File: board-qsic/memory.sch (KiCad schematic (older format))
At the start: 9 parts, among them U401 XC7A75T-CSG324, U501 IS43TR16128B

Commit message: Reworked board from template.  Changed schematic to let me use the bus drivers and level converters more efficiently so to get all the signals.
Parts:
- removed U401: XC7A75T-CSG324, myMods.pretty:CSG324, symbol myLib:XC7A75T-CSG324
- added C301, C302, C303: 100nF, Capacitor_SMD:C_0603_1608Metric, symbol Device:C_Small
- added U101: XC7A75T-CSG324, Package_BGA:BGA-324_15.0x15.0mm_Layout18x18_P0.8mm_Ball0.5mm_Pad0.4mm_NSMD, symbol FPGA_Xilinx_Artix7:XC7A75T-CSG324
- C304: renamed from C501; footprint Capacitors_SMD:C_0603 -> Capacitor_SMD:C_0603_1608Metric; symbol qsic-rescue:C_Small-device -> Device:C_Small; manf# (none) -> CL10B104KB8NNNL
- C305: renamed from C502; footprint Capacitors_SMD:C_0603 -> Capacitor_SMD:C_0603_1608Metric; symbol qsic-rescue:C_Small-device -> Device:C_Small; manf# (none) -> CL10B104KB8NNNL
- R301: renamed from R505; footprint Resistors_SMD:R_0603 -> Resistor_SMD:R_0603_1608Metric; symbol qsic-rescue:R-device -> Device:R; manf# (none) -> RC0603JR-07240RL
- R302: renamed from R502; footprint Resistors_SMD:R_0603 -> Resistor_SMD:R_0603_1608Metric; symbol qsic-rescue:R-device -> Device:R; manf# (none) -> RC0603FR-0788R7L
- R303: renamed from R501; footprint Resistors_SMD:R_0603 -> Resistor_SMD:R_0603_1608Metric; symbol qsic-rescue:R-device -> Device:R; manf# (none) -> RC0603FR-0747KL
- R304: renamed from R503; footprint Resistors_SMD:R_0603 -> Resistor_SMD:R_0603_1608Metric; symbol qsic-rescue:R-device -> Device:R; manf# (none) -> RC0603FR-0747RL
- R305: renamed from R504; footprint Resistors_SMD:R_0603 -> Resistor_SMD:R_0603_1608Metric; symbol qsic-rescue:R-device -> Device:R; manf# (none) -> RC0603FR-0747RL
- U301: renamed from U501; footprint Housings_BGA:BGA-96_2x3x16_9.0x13.0mm_Pitch0.8mm -> Package_BGA:BGA-96_9.0x13.0mm_Layout2x3x16_P0.8mm; manf# (none) -> IS43TR16128B-125KBL
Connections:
- net labels added: 1V5
- net labels removed: +1V5, A14
- wire segments 205 -> 227
- no-connect marks 1 -> 2
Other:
- moved on the sheet: U301A, U301B

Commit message: A few fixups from ERC.  Ground CS# on the memory chip.
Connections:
- net GND: now also U301.L2 (CS#)
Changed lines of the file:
@@
 	6525 4950 6625 5050
-Entry Wire Line
-	6525 5050 6625 5150
 Entry Wire Line
 	6525 5150 6625 5250
@@
 Wire Wire Line
 	7000 5250 6625 5250
-Wire Wire Line
-	7000 5150 6625 5150
 Wire Wire Line
 	7000 5050 6625 5050
@@
 	9400 3150 9400 3250
 Connection ~ 9525 1450
+$Comp
+L power:GND #PWR0152
+U 1 1 5DB3990D
+P 6750 5100
+F 0 "#PWR0152" H 6750 4850 50  0001 C CNN
+F 1 "GND" H 6750 4950 50  0001 C CNN
+F 2 "" H 6750 5100 50  0000 C CNN
+F 3 "" H 6750 5100 50  0000 C CNN
+	1    6750 5100
+	1    0    0    -1
+$EndComp
+Wire Wire Line
+	6750 5100 6900 5100
+Wire Wire Line
+	6900 5100 6900 5150
+Wire Wire Line
+	6900 5150 7000 5150
 Wire Bus Line
 	5000 1650 8575 1650

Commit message: Added 1% to the Vref voltage divider.
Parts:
- R304, R305: value 47 -> 47 1%
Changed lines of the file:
@@
 U 1 1 58C4D4F2
 P 8925 5900
-F 0 "R304" V 9005 5900 50  0000 C CNN
-F 1 "47" V 8925 5900 50  0000 C CNN
+F 0 "R304" H 8995 5946 50  0000 L CNN
+F 1 "47 1%" H 8995 5855 50  0000 L CNN
 F 2 "Resistor_SMD:R_0603_1608Metric" V 8855 5900 50  0001 C CNN
 F 3 "" H 8925 5900 50  0000 C CNN
@@
 U 1 1 58C4D525
 P 8925 6350
-F 0 "R305" V 9005 6350 50  0000 C CNN
-F 1 "47" V 8925 6350 50  0000 C CNN
+F 0 "R305" H 8995 6396 50  0000 L CNN
+F 1 "47 1%" H 8995 6305 50  0000 L CNN
 F 2 "Resistor_SMD:R_0603_1608Metric" V 8855 6350 50  0001 C CNN
 F 3 "" H 8925 6350 50  0000 C CNN

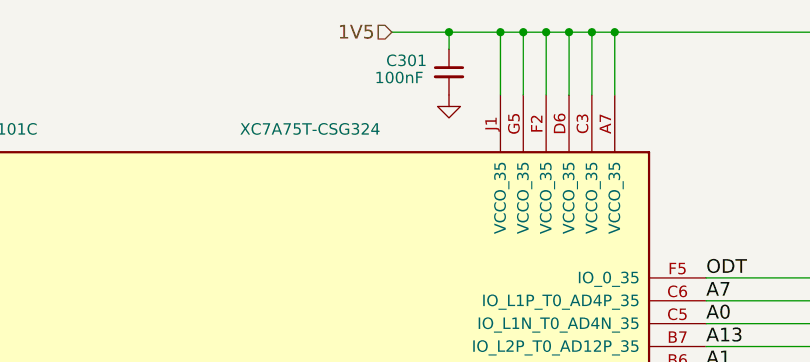
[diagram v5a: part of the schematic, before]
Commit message: Changed some capacitors from 100nF to 10uF
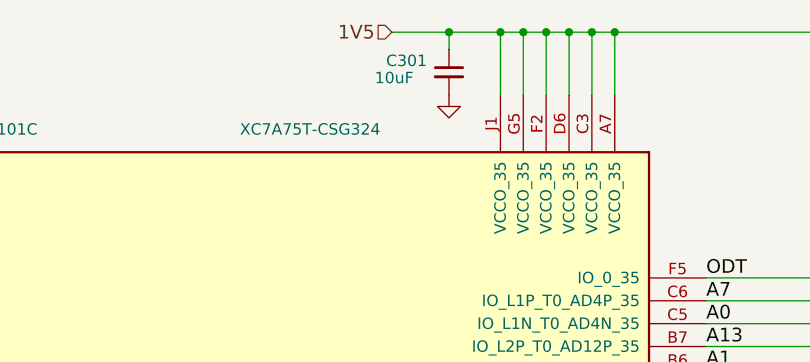
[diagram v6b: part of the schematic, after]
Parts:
- C301: value 100nF -> 10uF
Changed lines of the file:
@@
 EESchema Schematic File Version 4
-LIBS:qsic-cache
 EELAYER 30 0
 EELAYER END
@@
 P 3225 900
 F 0 "C301" H 2950 950 50  0000 L CNN
-F 1 "100nF" H 2900 875 50  0000 L CNN
+F 1 "10uF" H 2900 875 50  0000 L CNN
 F 2 "Capacitor_SMD:C_0603_1608Metric" H 3225 900 50  0001 C CNN
 F 3 "" H 3225 900 50  0000 C CNN

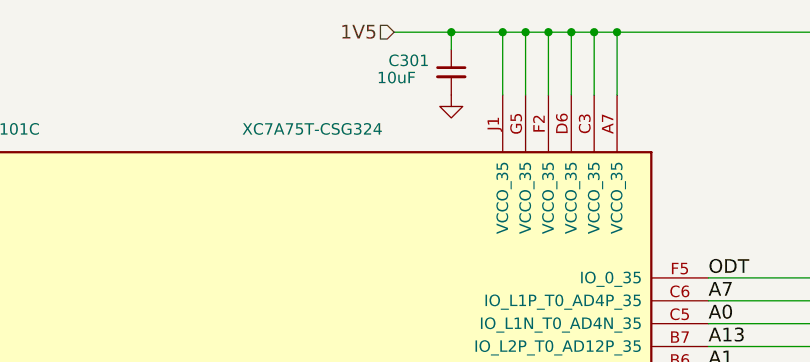
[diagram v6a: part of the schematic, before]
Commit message: These are all old changes in directories that are now historical.
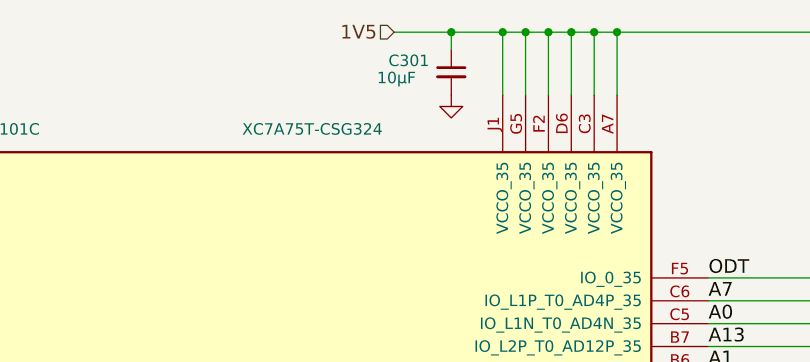
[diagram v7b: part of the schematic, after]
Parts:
- C301: value 10uF -> 10µF
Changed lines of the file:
@@
 P 3225 900
 F 0 "C301" H 2950 950 50  0000 L CNN
-F 1 "10uF" H 2900 875 50  0000 L CNN
+F 1 "10µF" H 2900 875 50  0000 L CNN
 F 2 "Capacitor_SMD:C_0603_1608Metric" H 3225 900 50  0001 C CNN
 F 3 "" H 3225 900 50  0000 C CNN
